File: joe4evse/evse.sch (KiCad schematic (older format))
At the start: 22 parts, among them U5 TC7660SxO, U6 UA741-D, U7 HCPL0731

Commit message: joe/sch: Assign footprints to components
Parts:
- C10: renamed from C8; footprint (none) -> Capacitor_SMD:C_0805_2012Metric
- C6: renamed from C5; footprint (none) -> Capacitor_SMD:C_0603_1608Metric
- C7: renamed from C6; footprint (none) -> Capacitor_SMD:C_0805_2012Metric
- C8: renamed from C10; footprint (none) -> Capacitor_SMD:C_0805_2012Metric
- C9: renamed from C7; footprint (none) -> Capacitor_SMD:C_0603_1608Metric
- R10: renamed from R31; footprint (none) -> Resistor_SMD:R_0603_1608Metric
- R11: renamed from R32; footprint (none) -> Resistor_SMD:R_0603_1608Metric
- R12: renamed from R33; footprint (none) -> Resistor_SMD:R_0603_1608Metric
- R13: renamed from R34; footprint (none) -> Resistor_SMD:R_0603_1608Metric
- R14: renamed from R35; footprint (none) -> Resistor_SMD:R_0603_1608Metric
- R15: renamed from R36; footprint (none) -> Resistor_SMD:R_0603_1608Metric
- R16: renamed from R37; footprint (none) -> Resistor_SMD:R_0603_1608Metric
- R17: renamed from R38; footprint (none) -> Resistor_SMD:R_0603_1608Metric
- R18: renamed from R39; footprint (none) -> Resistor_SMD:R_0603_1608Metric
- R19: renamed from R40; footprint (none) -> Resistor_SMD:R_0603_1608Metric
- renumbered D31 to D10, D32 to D11, D33 to D12, D34 to D13

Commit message: joe/sch: Remove relays and only keep control circuitry
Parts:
- removed D11, D12: 1N4001, Diode_THT:D_DO-41_SOD81_P10.16mm_Horizontal, symbol Diode:1N4001
- added D11, D12: S1A-13-F, Diode_SMD:D_SMA, symbol ma4evse:S1A-13-F
- added R20, R21: 100k, Resistor_SMD:R_1206_3216Metric, symbol Device:R_Small
- D13: footprint Diode_THT:D_DO-35_SOD27_P7.62mm_Horizontal -> Diode_SMD:D_SOD-323
- R16, R17: value 200k -> 100k; footprint Resistor_SMD:R_0603_1608Metric -> Resistor_SMD:R_1206_3216Metric
- U5, U6, U7: footprint Package_SO:SO-8_3.9x4.9mm_P1.27mm -> Package_SO:SOIC-8_3.9x4.9mm_P1.27mm
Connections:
- wire segments 71 -> 73
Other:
- note added: "Two resistors are put in series to get a\nhigh voltage rating, as this is 230VAC.\nUse at least 1206 package, as it usually\ncan handle at least 300V."
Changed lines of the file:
@@
 $Descr A4 11693 8268
 encoding utf-8
-Sheet 6 6
+Sheet 6 3
 Title "Joe 4 EVSE"
 Date "2019-12-10"
@@
 F 0 "U6" H 6850 1700 50  0000 L CNN
 F 1 "UA741-D" H 6850 1800 50  0000 L CNN
-F 2 "Package_SO:SO-8_3.9x4.9mm_P1.27mm" H 6750 2000 50  0001 C CNN
+F 2 "Package_SO:SOIC-8_3.9x4.9mm_P1.27mm" H 6750 2000 50  0001 C CNN
 F 3 "https://www.ti.com/lit/ds/slos094g/slos094g.pdf" H 6750 2100 50  0001 C CNN
 	1    6700 1950
@@
 F 0 "U7" H 5900 4967 50  0000 C CNN
 F 1 "HCPL0731" H 5900 4876 50  0000 C CNN
-F 2 "Package_SO:SO-8_3.9x4.9mm_P1.27mm" H 5875 4450 50  0001 C CNN
+F 2 "Package_SO:SOIC-8_3.9x4.9mm_P1.27mm" H 5875 4450 50  0001 C CNN
 F 3 "http://www.onsemi.com/pub/Collateral/HCPL2731-D.pdf" H 5875 4450 50  0001 C CNN
 	1    5900 4450
 	1    0    0    -1
-$EndComp
-$Comp
-L Diode:1N4001 D11
-U 1 1 5DF52C39
-P 5250 4150
-F 0 "D11" H 5250 3934 50  0000 C CNN
-F 1 "1N4001" H 5250 4025 50  0000 C CNN
-F 2 "Diode_THT:D_DO-41_SOD81_P10.16mm_Horizontal" H 5250 3975 50  0001 C CNN
-F 3 "http://www.vishay.com/docs/88503/1n4001.pdf" H 5250 4150 50  0001 C CNN
-	1    5250 4150
-	-1   0    0    1
-$EndComp
-$Comp
-L Diode:1N4001 D12
-U 1 1 5DF54676
-P 5250 4750
-F 0 "D12" H 5250 4534 50  0000 C CNN
-F 1 "1N4001" H 5250 4625 50  0000 C CNN
-F 2 "Diode_THT:D_DO-41_SOD81_P10.16mm_Horizontal" H 5250 4575 50  0001 C CNN
-F 3 "http://www.vishay.com/docs/88503/1n4001.pdf" H 5250 4750 50  0001 C CNN
-	1    5250 4750
-	-1   0    0    1
 $EndComp
 Wire Wire Line
@@
 P 4900 4150
 F 0 "R16" V 4704 4150 50  0000 C CNN
-F 1 "200k" V 4795 4150 50  0000 C CNN
-F 2 "Resistor_SMD:R_0603_1608Metric" H 4900 4150 50  0001 C CNN
+F 1 "100k" V 4795 4150 50  0000 C CNN
+F 2 "Resistor_SMD:R_1206_3216Metric" H 4900 4150 50  0001 C CNN
 F 3 "~" H 4900 4150 50  0001 C CNN
 	1    4900 4150
@@
 P 4900 4750
 F 0 "R17" V 4704 4750 50  0000 C CNN
-F 1 "200k" V 4795 4750 50  0000 C CNN
-F 2 "Resistor_SMD:R_0603_1608Metric" H 4900 4750 50  0001 C CNN
+F 1 "100k" V 4795 4750 50  0000 C CNN
+F 2 "Resistor_SMD:R_1206_3216Metric" H 4900 4750 50  0001 C CNN
 F 3 "~" H 4900 4750 50  0001 C CNN
 	1    4900 4750
@@
 Wire Wire Line
 	5100 4150 5000 4150
-Text Label 4200 4150 0    50   ~ 0
+Text Label 3900 4150 0    50   ~ 0
 AC_TEST_IN0
-Text Label 4200 4750 0    50   ~ 0
+Text Label 3900 4750 0    50   ~ 0
 AC_TEST_IN1
 Wire Wire Line
-	4200 4150 4800 4150
-Wire Wire Line
-	4200 4750 4800 4750
+	3900 4150 4500 4150
+Wire Wire Line
+	3900 4750 4500 4750
 $Comp
 L power:GND #PWR066
@@
 F 0 "D13" V 5354 6829 50  0000 L CNN
 F 1 "1N4148" V 5445 6829 50  0000 L CNN
-F 2 "Diode_THT:D_DO-35_SOD27_P7.62mm_Horizontal" H 5400 6575 50  0001 C CNN
+F 2 "Diode_SMD:D_SOD-323" H 5400 6575 50  0001 C CNN
 F 3 "https://assets.nexperia.com/documents/data-sheet/1N4148_1N4448.pdf" H 5400 6750 50  0001 C CNN
 	1    5400 6750
@@
 F 0 "U5" H 3400 2550 50  0000 C CNN
 F 1 "TC7660SxO" H 3400 2450 50  0000 C CNN
-F 2 "Package_SO:SO-8_3.9x4.9mm_P1.27mm" H 3850 1850 50  0001 C CNN
+F 2 "Package_SO:SOIC-8_3.9x4.9mm_P1.27mm" H 3850 1850 50  0001 C CNN
 F 3 "http://ww1.microchip.com/downloads/en/DeviceDoc/21468B.pdf" H 3850 1850 50  0001 C CNN
 	1    3750 1950
@@
 Wire Wire Line
 	3100 2150 3100 2650
+$Comp
+L ma4evse:S1A-13-F D11
+U 1 1 5E2401D6
+P 5250 4150
+F 0 "D11" H 5250 3934 50  0000 C CNN
+F 1 "S1A-13-F" H 5250 4025 50  0000 C CNN
+F 2 "Diode_SMD:D_SMA" H 5250 3975 50  0001 C CNN
+F 3 "https://www.diodes.com/assets/Datasheets/ds16003.pdf" H 5250 4150 50  0001 C CNN
+	1    5250 4150
+	-1   0    0    1
+$EndComp
+$Comp
+L ma4evse:S1A-13-F D12
+U 1 1 5E242A7A
+P 5250 4750
+F 0 "D12" H 5250 4534 50  0000 C CNN
+F 1 "S1A-13-F" H 5250 4625 50  0000 C CNN
+F 2 "Diode_SMD:D_SMA" H 5250 4575 50  0001 C CNN
+F 3 "https://www.diodes.com/assets/Datasheets/ds16003.pdf" H 5250 4750 50  0001 C CNN
+	1    5250 4750
+	-1   0    0    1
+$EndComp
+$Comp
+L Device:R_Small R20
+U 1 1 5E24E069
+P 4600 4150
+F 0 "R20" V 4404 4150 50  0000 C CNN
+F 1 "100k" V 4495 4150 50  0000 C CNN
+F 2 "Resistor_SMD:R_1206_3216Metric" H 4600 4150 50  0001 C CNN
+F 3 "~" H 4600 4150 50  0001 C CNN
+	1    4600 4150
+	0    1    1    0
+$EndComp
+$Comp
+L Device:R_Small R21
+U 1 1 5E24E314
+P 4600 4750
+F 0 "R21" V 4404 4750 50  0000 C CNN
+F 1 "100k" V 4495 4750 50  0000 C CNN
+F 2 "Resistor_SMD:R_1206_3216Metric" H 4600 4750 50  0001 C CNN
+F 3 "~" H 4600 4750 50  0001 C CNN
+	1    4600 4750
+	0    1    1    0
+$EndComp
+Wire Wire Line
+	4700 4150 4800 4150
+Wire Wire Line
+	4800 4750 4700 4750
+Text Notes 3750 5250 0    50   ~ 0
+Two resistors are put in series to get a\nhigh voltage rating, as this is 230VAC.\nUse at least 1206 package, as it usually\ncan handle at least 300V.
 $EndSCHEMATC

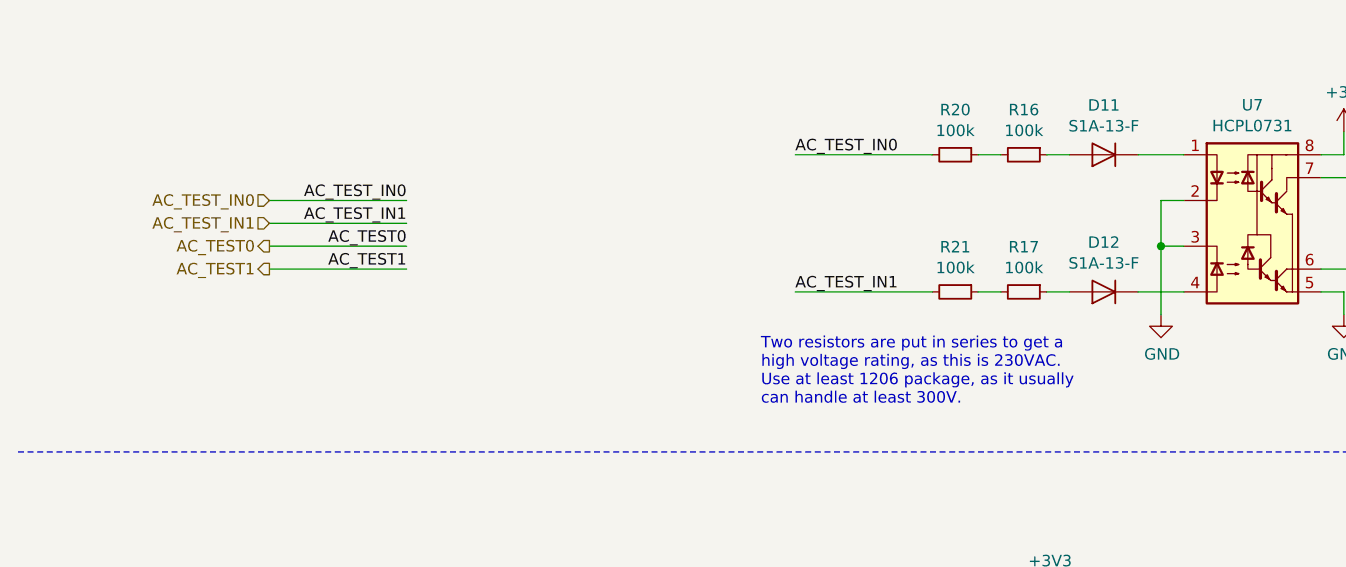
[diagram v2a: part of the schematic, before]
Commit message: joe/sch: Remove relays and reference AC test to neutral rather than GND
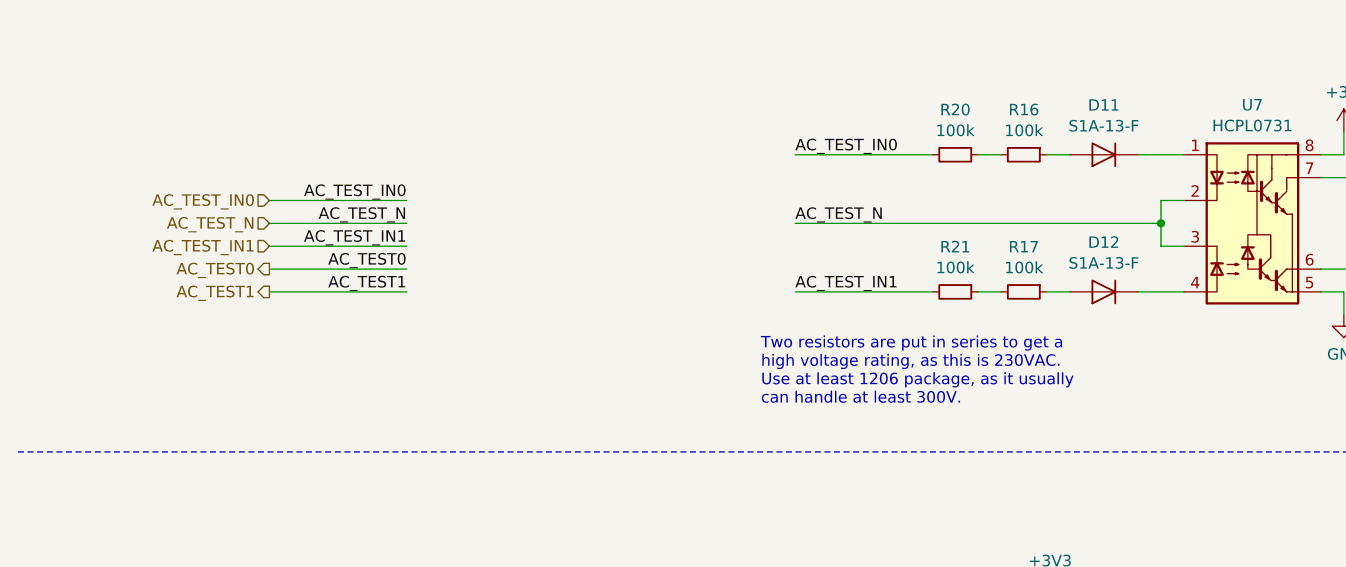
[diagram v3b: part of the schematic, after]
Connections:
- net GND: no longer U7.2 (C1), U7.3 (C2)
- new net AC_TEST_N: U7.2 (C1), U7.3 (C2)
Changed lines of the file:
@@
 $Descr A4 11693 8268
 encoding utf-8
-Sheet 6 3
+Sheet 3 3
 Title "Joe 4 EVSE"
 Date "2019-12-10"
@@
 	5600 4350 5500 4350
 Wire Wire Line
-	5500 4350 5500 4550
+	5500 4350 5500 4450
 Wire Wire Line
 	5600 4550 5500 4550
-Connection ~ 5500 4550
-Wire Wire Line
-	5500 4550 5500 4850
 $Comp
 L Device:R_Small R16
@@
 Wire Wire Line
 	3900 4750 4500 4750
-$Comp
-L power:GND #PWR066
-U 1 1 5DF5D9A3
-P 5500 4850
-F 0 "#PWR066" H 5500 4600 50  0001 C CNN
-F 1 "GND" H 5505 4677 50  0000 C CNN
-F 2 "" H 5500 4850 50  0001 C CNN
-F 3 "" H 5500 4850 50  0001 C CNN
-	1    5500 4850
-	1    0    0    -1
-$EndComp
 $Comp
 L power:GND #PWR067
@@
 Text Label 2200 4350 2    50   ~ 0
 AC_TEST_IN0
-Text Label 2200 4450 2    50   ~ 0
+Text Label 2200 4550 2    50   ~ 0
 AC_TEST_IN1
 Wire Wire Line
 	2200 4350 1600 4350
 Wire Wire Line
-	2200 4450 1600 4450
-Wire Wire Line
-	1600 4550 2200 4550
+	2200 4550 1600 4550
 Wire Wire Line
 	1600 4650 2200 4650
-Text Label 2200 4550 2    50   ~ 0
+Wire Wire Line
+	1600 4750 2200 4750
+Text Label 2200 4650 2    50   ~ 0
 AC_TEST0
-Text Label 2200 4650 2    50   ~ 0
+Text Label 2200 4750 2    50   ~ 0
 AC_TEST1
 Wire Wire Line
@@
 Text HLabel 1600 4350 0    50   Input ~ 0
 AC_TEST_IN0
-Text HLabel 1600 4450 0    50   Input ~ 0
+Text HLabel 1600 4550 0    50   Input ~ 0
 AC_TEST_IN1
-Text HLabel 1600 4550 0    50   Output ~ 0
+Text HLabel 1600 4650 0    50   Output ~ 0
 AC_TEST0
-Text HLabel 1600 4650 0    50   Output ~ 0
+Text HLabel 1600 4750 0    50   Output ~ 0
 AC_TEST1
 Text HLabel 1750 6450 0    50   Input ~ 0
@@
 Text Notes 3750 5250 0    50   ~ 0
 Two resistors are put in series to get a\nhigh voltage rating, as this is 230VAC.\nUse at least 1206 package, as it usually\ncan handle at least 300V.
+Wire Wire Line
+	5500 4450 3900 4450
+Connection ~ 5500 4450
+Wire Wire Line
+	5500 4450 5500 4550
+Text Label 3900 4450 0    50   ~ 0
+AC_TEST_N
+Wire Wire Line
+	1600 4450 2200 4450
+Text Label 2200 4450 2    50   ~ 0
+AC_TEST_N
+Text HLabel 1600 4450 0    50   Input ~ 0
+AC_TEST_N
 $EndSCHEMATC

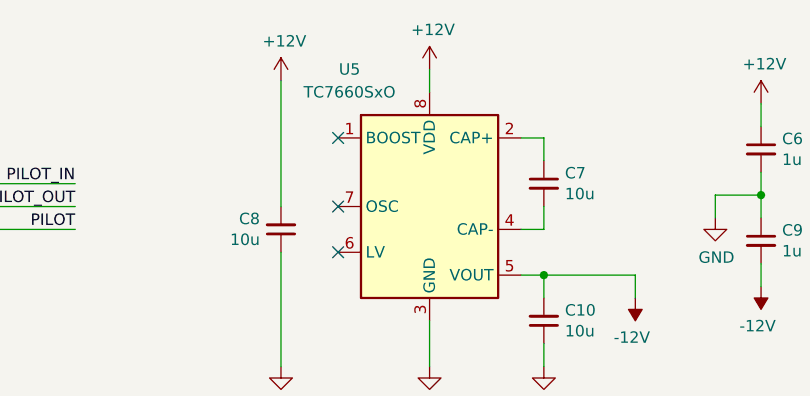
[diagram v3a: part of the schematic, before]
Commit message: joe/*: Connect charge pump boost pin to +12V
This increases the switching frequency from 10kHz to 45kHz, making the
pump capacitor resonating inaudible.
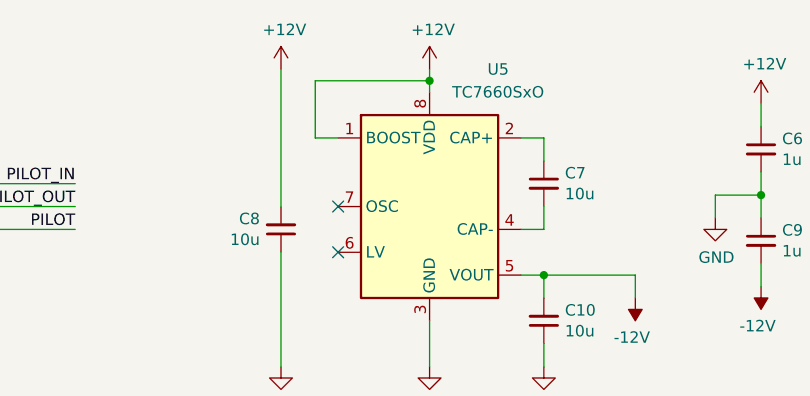
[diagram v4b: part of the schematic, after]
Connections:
- net +12V: now also U5.1 (BOOST)
- no-connect marks 5 -> 4
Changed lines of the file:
@@
 PP_READ
-$Comp
-L ma4evse:TC7660SxO U5
-U 1 1 5DF73610
-P 3750 1950
-F 0 "U5" H 3400 2550 50  0000 C CNN
-F 1 "TC7660SxO" H 3400 2450 50  0000 C CNN
-F 2 "Package_SO:SOIC-8_3.9x4.9mm_P1.27mm" H 3850 1850 50  0001 C CNN
-F 3 "http://ww1.microchip.com/downloads/en/DeviceDoc/21468B.pdf" H 3850 1850 50  0001 C CNN
-	1    3750 1950
-	1    0    0    -1
-$EndComp
 $Comp
 L power:GND #PWR063
@@
 NoConn ~ 3350 2150
 Wire Wire Line
-	3750 1350 3750 1450
-NoConn ~ 3350 1650
+	3750 1350 3750 1400
 Wire Wire Line
 	4150 2250 4250 2250
@@
 L power:+12V #PWR050
 U 1 1 5E20B3B1
-P 3100 1400
-F 0 "#PWR050" H 3100 1250 50  0001 C CNN
-F 1 "+12V" H 3115 1573 50  0000 C CNN
-F 2 "" H 3100 1400 50  0001 C CNN
-F 3 "" H 3100 1400 50  0001 C CNN
-	1    3100 1400
-	1    0    0    -1
-$EndComp
-Wire Wire Line
-	3100 1400 3100 1950
+P 3100 1350
+F 0 "#PWR050" H 3100 1200 50  0001 C CNN
+F 1 "+12V" H 3115 1523 50  0000 C CNN
+F 2 "" H 3100 1350 50  0001 C CNN
+F 3 "" H 3100 1350 50  0001 C CNN
+	1    3100 1350
+	1    0    0    -1
+$EndComp
+Wire Wire Line
+	3100 1350 3100 1950
 $Comp
 L power:GND #PWR062
@@
 Text HLabel 1600 4450 0    50   Input ~ 0
 AC_TEST_N
+$Comp
+L ma4evse:TC7660SxO U5
+U 1 1 5DF73610
+P 3750 1950
+F 0 "U5" H 4050 2550 50  0000 C CNN
+F 1 "TC7660SxO" H 4050 2450 50  0000 C CNN
+F 2 "Package_SO:SOIC-8_3.9x4.9mm_P1.27mm" H 3850 1850 50  0001 C CNN
+F 3 "http://ww1.microchip.com/downloads/en/DeviceDoc/21468B.pdf" H 3850 1850 50  0001 C CNN
+	1    3750 1950
+	1    0    0    -1
+$EndComp
+Wire Wire Line
+	3350 1650 3250 1650
+Wire Wire Line
+	3250 1650 3250 1400
+Wire Wire Line
+	3250 1400 3750 1400
+Connection ~ 3750 1400
+Wire Wire Line
+	3750 1400 3750 1450
 $EndSCHEMATC

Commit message: joe/pcb: Fix D13 footprint
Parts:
- D13: footprint Diode_SMD:D_SOD-323 -> Diode_SMD:D_SOD-123
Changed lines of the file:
@@
 F 0 "D13" V 5354 6829 50  0000 L CNN
 F 1 "1N4148" V 5445 6829 50  0000 L CNN
-F 2 "Diode_SMD:D_SOD-323" H 5400 6575 50  0001 C CNN
+F 2 "Diode_SMD:D_SOD-123" H 5400 6575 50  0001 C CNN
 F 3 "https://assets.nexperia.com/documents/data-sheet/1N4148_1N4448.pdf" H 5400 6750 50  0001 C CNN
 	1    5400 6750

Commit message: joe/{sch, pcb}: Add 0r resistors in parallel of SW1 for prod boards
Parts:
- U6: Manufacturer (none) -> Ti; Manufacturer PN (none) -> uA741-D
- U7: Manufacturer (none) -> ON Semi; Manufacturer PN (none) -> HCPL0731
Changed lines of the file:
@@
 F 2 "Package_SO:SOIC-8_3.9x4.9mm_P1.27mm" H 6750 2000 50  0001 C CNN
 F 3 "https://www.ti.com/lit/ds/slos094g/slos094g.pdf" H 6750 2100 50  0001 C CNN
+F 4 "Ti" H 6700 1950 50  0001 C CNN "Manufacturer"
+F 5 "uA741-D" H 6700 1950 50  0001 C CNN "Manufacturer PN"
 	1    6700 1950
 	1    0    0    -1
@@
 F 2 "Package_SO:SOIC-8_3.9x4.9mm_P1.27mm" H 5875 4450 50  0001 C CNN
 F 3 "http://www.onsemi.com/pub/Collateral/HCPL2731-D.pdf" H 5875 4450 50  0001 C CNN
+F 4 "ON Semi" H 5900 4450 50  0001 C CNN "Manufacturer"
+F 5 "HCPL0731" H 5900 4450 50  0001 C CNN "Manufacturer PN"
 	1    5900 4450
 	1    0    0    -1
